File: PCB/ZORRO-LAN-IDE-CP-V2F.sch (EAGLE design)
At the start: 77 parts, among them CN1 ZORROII_EDGE_ROUND_CONTACTS, CN2 A1200-CLOCKPORT, IC1 ENC624J600, IC2 XC95288XL-TQ144, IC3 74HCT245PW, IC4 74HCT245PW, IC5 74HCT245PW, IC7 LD117ADT33TR, IC8 AM29F010S, Q1 25MHz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

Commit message: Update in Firmware (pure Z2-AC but LAN becomes Z3) and new pcb
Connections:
- removed net LAN_CGF2: IC2.P$135-FB6MC02
- net INT6: now also IC2.P$135-FB6MC02
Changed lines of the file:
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@@
 </segment>
 </net>
-<net name="LAN_CGF2" class="0">
+<net name="INT6" class="0">
 <segment>
 <pinref part="IC2" gate="G$1" pin="P$135-FB6MC02"/>

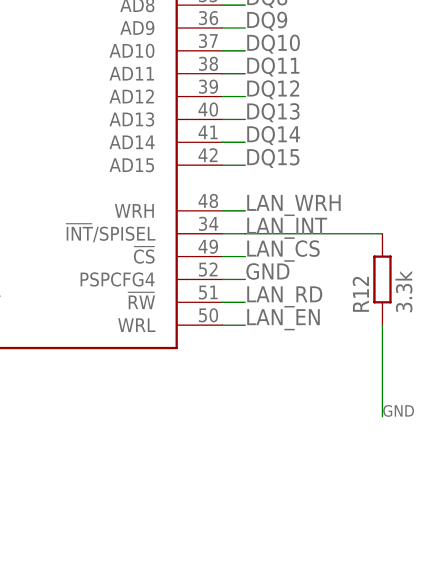
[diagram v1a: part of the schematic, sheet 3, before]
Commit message: Firmware for new version. IDE and CP working
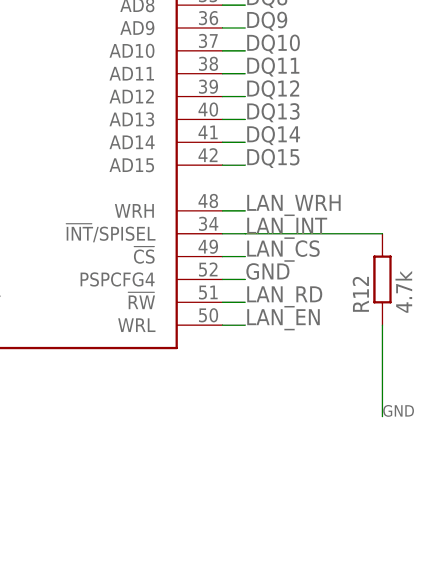
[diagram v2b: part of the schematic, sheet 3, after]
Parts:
- C20, C31: device rcl:C-EUC1210K -> rcl:C-EUC1206K
- R12: value 3.3k -> 4.7k
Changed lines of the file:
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@@
 <?xml version="1.0" encoding="utf-8"?>
 <!DOCTYPE eagle SYSTEM "eagle.dtd">
-<eagle version="6.5.0">
+<eagle version="6.6.0">
 <drawing>
 <settings>
@@
 <grid distance="0.1" unitdist="inch" unit="inch" style="lines" multiple="1" display="no" altdistance="0.01" altunitdist="inch" altunit="inch"/>
 <layers>
-<layer number="1" name="Top" color="4" fill="1" visible="no" active="no"/>
-<layer number="2" name="Route2" color="1" fill="3" visible="no" active="no"/>
-<layer number="3" name="Route3" color="4" fill="3" visible="no" active="no"/>
-<layer number="4" name="Route4" color="1" fill="4" visible="no" active="no"/>
-<layer number="5" name="Route5" color="4" fill="4" visible="no" active="no"/>
-<layer number="6" name="Route6" color="1" fill="8" visible="no" active="no"/>
-<layer number="7" name="Route7" color="4" fill="8" visible="no" active="no"/>
-<layer number="8" name="Route8" color="1" fill="2" visible="no" active="no"/>
-<layer number="9" name="Route9" color="4" fill="2" visible="no" active="no"/>
-<layer number="10" name="Route10" color="1" fill="7" visible="no" active="no"/>
-<layer number="11" name="Route11" color="4" fill="7" visible="no" active="no"/>
-<layer number="12" name="Route12" color="1" fill="5" visible="no" active="no"/>
-<layer number="13" name="Route13" color="4" fill="5" visible="no" active="no"/>
-<layer number="14" name="Route14" color="1" fill="6" visible="no" active="no"/>
-<layer number="15" name="Route15" color="4" fill="6" visible="no" active="no"/>
-<layer number="16" name="Bottom" color="1" fill="1" visible="no" active="no"/>
-<layer number="17" name="Pads" color="2" fill="1" visible="no" active="no"/>
-<layer number="18" name="Vias" color="2" fill="1" visible="no" active="no"/>
-<layer number="19" name="Unrouted" color="6" fill="1" visible="no" active="no"/>
-<layer number="20" name="Dimension" color="15" fill="1" visible="no" active="no"/>
-<layer number="21" name="tPlace" color="7" fill="1" visible="no" active="no"/>
-<layer number="22" name="bPlace" color="7" fill="1" visible="no" active="no"/>
-<layer number="23" name="tOrigins" color="15" fill="1" visible="no" active="no"/>
-<layer number="24" name="bOrigins" color="15" fill="1" visible="no" active="no"/>
-<layer number="25" name="tNames" color="7" fill="1" visible="no" active="no"/>
-<layer number="26" name="bNames" color="7" fill="1" visible="no" active="no"/>
-<layer number="27" name="tValues" color="7" fill="1" visible="no" active="no"/>
-<layer number="28" name="bValues" color="7" fill="1" visible="no" active="no"/>
+<layer number="1" name="Top" color="4" fill="1" visible="yes" active="no"/>
+<layer number="2" name="Route2" color="1" fill="3" visible="yes" active="no"/>
+<layer number="3" name="Route3" color="4" fill="3" visible="yes" active="no"/>
+<layer number="4" name="Route4" color="1" fill="4" visible="yes" active="no"/>
+<layer number="5" name="Route5" color="4" fill="4" visible="yes" active="no"/>
+<layer number="6" name="Route6" color="1" fill="8" visible="yes" active="no"/>
+<layer number="7" name="Route7" color="4" fill="8" visible="yes" active="no"/>
+<layer number="8" name="Route8" color="1" fill="2" visible="yes" active="no"/>
+<layer number="9" name="Route9" color="4" fill="2" visible="yes" active="no"/>
+<layer number="10" name="Route10" color="1" fill="7" visible="yes" active="no"/>
+<layer number="11" name="Route11" color="4" fill="7" visible="yes" active="no"/>
+<layer number="12" name="Route12" color="1" fill="5" visible="yes" active="no"/>
+<layer number="13" name="Route13" color="4" fill="5" visible="yes" active="no"/>
+<layer number="14" name="Route14" color="1" fill="6" visible="yes" active="no"/>
+<layer number="15" name="Route15" color="4" fill="6" visible="yes" active="no"/>
+<layer number="16" name="Bottom" color="1" fill="1" visible="yes" active="no"/>
+<layer number="17" name="Pads" color="2" fill="1" visible="yes" active="no"/>
+<layer number="18" name="Vias" color="2" fill="1" visible="yes" active="no"/>
+<layer number="19" name="Unrouted" color="6" fill="1" visible="yes" active="no"/>
+<layer number="20" name="Dimension" color="15" fill="1" visible="yes" active="no"/>
+<layer number="21" name="tPlace" color="7" fill="1" visible="yes" active="no"/>
+<layer number="22" name="bPlace" color="7" fill="1" visible="yes" active="no"/>
+<layer number="23" name="tOrigins" color="15" fill="1" visible="yes" active="no"/>
+<layer number="24" name="bOrigins" color="15" fill="1" visible="yes" active="no"/>
+<layer number="25" name="tNames" color="7" fill="1" visible="yes" active="no"/>
+<layer number="26" name="bNames" color="7" fill="1" visible="yes" active="no"/>
+<layer number="27" name="tValues" color="7" fill="1" visible="yes" active="no"/>
+<layer number="28" name="bValues" color="7" fill="1" visible="yes" active="no"/>
 <layer number="29" name="tStop" color="7" fill="3" visible="no" active="no"/>
 <layer number="30" name="bStop" color="7" fill="6" visible="no" active="no"/>
@@
 <layer number="35" name="tGlue" color="7" fill="4" visible="no" active="no"/>
 <layer number="36" name="bGlue" color="7" fill="5" visible="no" active="no"/>
-<layer number="37" name="tTest" color="7" fill="1" visible="no" active="no"/>
-<layer number="38" name="bTest" color="7" fill="1" visible="no" active="no"/>
+<layer number="37" name="tTest" color="7" fill="1" visible="yes" active="no"/>
+<layer number="38" name="bTest" color="7" fill="1" visible="yes" active="no"/>
 <layer number="39" name="tKeepout" color="4" fill="11" visible="no" active="no"/>
 <layer number="40" name="bKeepout" color="1" fill="11" visible="no" active="no"/>
@@
 <layer number="44" name="Drills" color="7" fill="1" visible="no" active="no"/>
 <layer number="45" name="Holes" color="7" fill="1" visible="no" active="no"/>
-<layer number="46" name="Milling" color="3" fill="1" visible="no" active="no"/>
-<layer number="47" name="Measures" color="7" fill="1" visible="no" active="no"/>
-<layer number="48" name="Document" color="7" fill="1" visible="no" active="no"/>
-<layer number="49" name="Reference" color="7" fill="1" visible="no" active="no"/>
-<layer number="50" name="dxf" color="7" fill="1" visible="no" active="no"/>
-<layer number="51" name="tDocu" color="7" fill="1" visible="no" active="no"/>
-<layer number="52" name="bDocu" color="7" fill="1" visible="no" active="no"/>
-<layer number="53" name="tGND_GNDA" color="7" fill="1" visible="no" active="no"/>
-<layer number="54" name="bGND_GNDA" color="7" fill="1" visible="no" active="no"/>
-<layer number="56" name="wert" color="7" fill="1" visible="no" active="no"/>
+<layer number="46" name="Milling" color="3" fill="1" visible="yes" active="no"/>
+<layer number="47" name="Measures" color="7" fill="1" visible="yes" active="no"/>
+<layer number="48" name="Document" color="7" fill="1" visible="yes" active="no"/>
+<layer number="49" name="Reference" color="7" fill="1" visible="yes" active="no"/>
+<layer number="50" name="dxf" color="7" fill="1" visible="yes" active="no"/>
+<layer number="51" name="tDocu" color="7" fill="1" visible="yes" active="no"/>
+<layer number="52" name="bDocu" color="7" fill="1" visible="yes" active="no"/>
+<layer number="53" name="tGND_GNDA" color="7" fill="1" visible="yes" active="no"/>
+<layer number="54" name="bGND_GNDA" color="7" fill="1" visible="yes" active="no"/>
+<layer number="56" name="wert" color="7" fill="1" visible="yes" active="no"/>
 <layer number="91" name="Nets" color="2" fill="1" visible="yes" active="yes"/>
 <layer number="92" name="Busses" color="1" fill="1" visible="yes" active="yes"/>
@@
 <part name="GND31" library="supply1" deviceset="GND" device=""/>
 <part name="P+3" library="supply1" deviceset="+5V" device=""/>
-<part name="C20" library="rcl" deviceset="C-EU" device="C1210K" value="10u"/>
+<part name="C20" library="rcl" deviceset="C-EU" device="C1206K" value="10u"/>
 <part name="GND32" library="supply1" deviceset="GND" device=""/>
 <part name="C21" library="rcl" deviceset="C-EU" device="C1210K" value="10u"/>
@@
 <part name="FRAME3" library="frames" deviceset="A4L-LOC" device=""/>
 <part name="R11" library="rcl" deviceset="R-EU_" device="R0805" value="1K"/>
-<part name="R12" library="rcl" deviceset="R-EU_" device="R0603" value="3.3k"/>
+<part name="R12" library="rcl" deviceset="R-EU_" device="R0603" value="4.7k"/>
 <part name="IC1" library="OLIMEX-ENJ" deviceset="ENC624J600" device=""/>
 <part name="C1" library="rcl" deviceset="C-EU" device="C0805K" value="100nF"/>
@@
 <part name="LEDB" library="jumper" deviceset="JP1E" device=""/>
 <part name="LEDA" library="jumper" deviceset="JP1E" device=""/>
-<part name="C31" library="rcl" deviceset="C-EU" device="C1210K" value="47u"/>
+<part name="C31" library="rcl" deviceset="C-EU" device="C1206K" value="47u"/>
 <part name="C32" library="rcl" deviceset="C-EU" device="C0603K" value="100n"/>
 <part name="Q2" library="crystal" deviceset="CRYSTAL" device="HC49UP" value="25MHz"/>

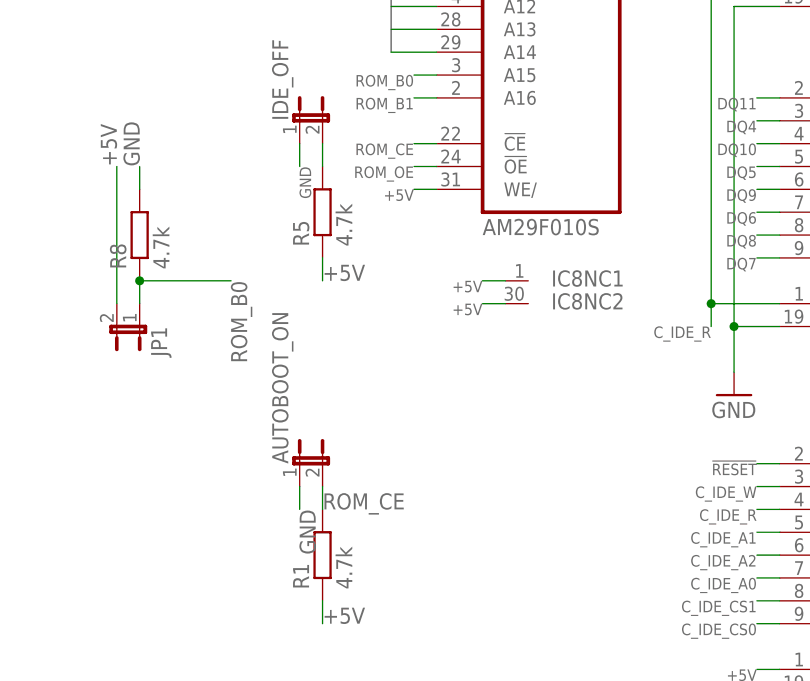
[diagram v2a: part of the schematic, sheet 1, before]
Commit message: Improved clock startup and IDE-ROM-timing
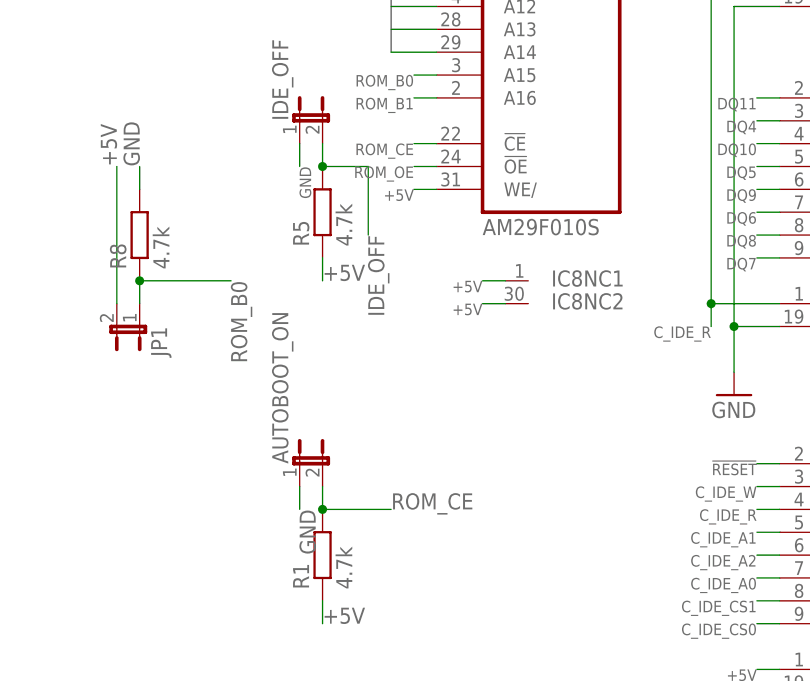
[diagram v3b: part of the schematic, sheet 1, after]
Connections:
- net AUTO_BOOT_OFF renamed IDE_OFF
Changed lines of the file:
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@@
 <grid distance="0.1" unitdist="inch" unit="inch" style="lines" multiple="1" display="no" altdistance="0.01" altunitdist="inch" altunit="inch"/>
 <layers>
-<layer number="1" name="Top" color="4" fill="1" visible="yes" active="no"/>
-<layer number="2" name="Route2" color="1" fill="3" visible="yes" active="no"/>
-<layer number="3" name="Route3" color="4" fill="3" visible="yes" active="no"/>
-<layer number="4" name="Route4" color="1" fill="4" visible="yes" active="no"/>
-<layer number="5" name="Route5" color="4" fill="4" visible="yes" active="no"/>
-<layer number="6" name="Route6" color="1" fill="8" visible="yes" active="no"/>
-<layer number="7" name="Route7" color="4" fill="8" visible="yes" active="no"/>
-<layer number="8" name="Route8" color="1" fill="2" visible="yes" active="no"/>
-<layer number="9" name="Route9" color="4" fill="2" visible="yes" active="no"/>
-<layer number="10" name="Route10" color="1" fill="7" visible="yes" active="no"/>
-<layer number="11" name="Route11" color="4" fill="7" visible="yes" active="no"/>
-<layer number="12" name="Route12" color="1" fill="5" visible="yes" active="no"/>
-<layer number="13" name="Route13" color="4" fill="5" visible="yes" active="no"/>
-<layer number="14" name="Route14" color="1" fill="6" visible="yes" active="no"/>
-<layer number="15" name="Route15" color="4" fill="6" visible="yes" active="no"/>
-<layer number="16" name="Bottom" color="1" fill="1" visible="yes" active="no"/>
-<layer number="17" name="Pads" color="2" fill="1" visible="yes" active="no"/>
-<layer number="18" name="Vias" color="2" fill="1" visible="yes" active="no"/>
-<layer number="19" name="Unrouted" color="6" fill="1" visible="yes" active="no"/>
-<layer number="20" name="Dimension" color="15" fill="1" visible="yes" active="no"/>
-<layer number="21" name="tPlace" color="7" fill="1" visible="yes" active="no"/>
-<layer number="22" name="bPlace" color="7" fill="1" visible="yes" active="no"/>
-<layer number="23" name="tOrigins" color="15" fill="1" visible="yes" active="no"/>
-<layer number="24" name="bOrigins" color="15" fill="1" visible="yes" active="no"/>
-<layer number="25" name="tNames" color="7" fill="1" visible="yes" active="no"/>
-<layer number="26" name="bNames" color="7" fill="1" visible="yes" active="no"/>
-<layer number="27" name="tValues" color="7" fill="1" visible="yes" active="no"/>
-<layer number="28" name="bValues" color="7" fill="1" visible="yes" active="no"/>
+<layer number="1" name="Top" color="4" fill="1" visible="no" active="no"/>
+<layer number="2" name="Route2" color="1" fill="3" visible="no" active="no"/>
+<layer number="3" name="Route3" color="4" fill="3" visible="no" active="no"/>
+<layer number="4" name="Route4" color="1" fill="4" visible="no" active="no"/>
+<layer number="5" name="Route5" color="4" fill="4" visible="no" active="no"/>
+<layer number="6" name="Route6" color="1" fill="8" visible="no" active="no"/>
+<layer number="7" name="Route7" color="4" fill="8" visible="no" active="no"/>
+<layer number="8" name="Route8" color="1" fill="2" visible="no" active="no"/>
+<layer number="9" name="Route9" color="4" fill="2" visible="no" active="no"/>
+<layer number="10" name="Route10" color="1" fill="7" visible="no" active="no"/>
+<layer number="11" name="Route11" color="4" fill="7" visible="no" active="no"/>
+<layer number="12" name="Route12" color="1" fill="5" visible="no" active="no"/>
+<layer number="13" name="Route13" color="4" fill="5" visible="no" active="no"/>
+<layer number="14" name="Route14" color="1" fill="6" visible="no" active="no"/>
+<layer number="15" name="Route15" color="4" fill="6" visible="no" active="no"/>
+<layer number="16" name="Bottom" color="1" fill="1" visible="no" active="no"/>
+<layer number="17" name="Pads" color="2" fill="1" visible="no" active="no"/>
+<layer number="18" name="Vias" color="2" fill="1" visible="no" active="no"/>
+<layer number="19" name="Unrouted" color="6" fill="1" visible="no" active="no"/>
+<layer number="20" name="Dimension" color="15" fill="1" visible="no" active="no"/>
+<layer number="21" name="tPlace" color="7" fill="1" visible="no" active="no"/>
+<layer number="22" name="bPlace" color="7" fill="1" visible="no" active="no"/>
+<layer number="23" name="tOrigins" color="15" fill="1" visible="no" active="no"/>
+<layer number="24" name="bOrigins" color="15" fill="1" visible="no" active="no"/>
+<layer number="25" name="tNames" color="7" fill="1" visible="no" active="no"/>
+<layer number="26" name="bNames" color="7" fill="1" visible="no" active="no"/>
+<layer number="27" name="tValues" color="7" fill="1" visible="no" active="no"/>
+<layer number="28" name="bValues" color="7" fill="1" visible="no" active="no"/>
 <layer number="29" name="tStop" color="7" fill="3" visible="no" active="no"/>
 <layer number="30" name="bStop" color="7" fill="6" visible="no" active="no"/>
@@
 <layer number="35" name="tGlue" color="7" fill="4" visible="no" active="no"/>
 <layer number="36" name="bGlue" color="7" fill="5" visible="no" active="no"/>
-<layer number="37" name="tTest" color="7" fill="1" visible="yes" active="no"/>
-<layer number="38" name="bTest" color="7" fill="1" visible="yes" active="no"/>
+<layer number="37" name="tTest" color="7" fill="1" visible="no" active="no"/>
+<layer number="38" name="bTest" color="7" fill="1" visible="no" active="no"/>
 <layer number="39" name="tKeepout" color="4" fill="11" visible="no" active="no"/>
 <layer number="40" name="bKeepout" color="1" fill="11" visible="no" active="no"/>
@@
 <layer number="44" name="Drills" color="7" fill="1" visible="no" active="no"/>
 <layer number="45" name="Holes" color="7" fill="1" visible="no" active="no"/>
-<layer number="46" name="Milling" color="3" fill="1" visible="yes" active="no"/>
-<layer number="47" name="Measures" color="7" fill="1" visible="yes" active="no"/>
-<layer number="48" name="Document" color="7" fill="1" visible="yes" active="no"/>
-<layer number="49" name="Reference" color="7" fill="1" visible="yes" active="no"/>
-<layer number="50" name="dxf" color="7" fill="1" visible="yes" active="no"/>
-<layer number="51" name="tDocu" color="7" fill="1" visible="yes" active="no"/>
-<layer number="52" name="bDocu" color="7" fill="1" visible="yes" active="no"/>
-<layer number="53" name="tGND_GNDA" color="7" fill="1" visible="yes" active="no"/>
-<layer number="54" name="bGND_GNDA" color="7" fill="1" visible="yes" active="no"/>
-<layer number="56" name="wert" color="7" fill="1" visible="yes" active="no"/>
+<layer number="46" name="Milling" color="3" fill="1" visible="no" active="no"/>
+<layer number="47" name="Measures" color="7" fill="1" visible="no" active="no"/>
+<layer number="48" name="Document" color="7" fill="1" visible="no" active="no"/>
+<layer number="49" name="Reference" color="7" fill="1" visible="no" active="no"/>
+<layer number="50" name="dxf" color="7" fill="1" visible="no" active="no"/>
+<layer number="51" name="tDocu" color="7" fill="1" visible="no" active="no"/>
+<layer number="52" name="bDocu" color="7" fill="1" visible="no" active="no"/>
+<layer number="53" name="tGND_GNDA" color="7" fill="1" visible="no" active="no"/>
+<layer number="54" name="bGND_GNDA" color="7" fill="1" visible="no" active="no"/>
+<layer number="56" name="wert" color="7" fill="1" visible="no" active="no"/>
 <layer number="91" name="Nets" color="2" fill="1" visible="yes" active="yes"/>
 <layer number="92" name="Busses" color="1" fill="1" visible="yes" active="yes"/>
@@
 </segment>
 </net>
-<net name="AUTO_BOOT_OFF" class="0">
+<net name="IDE_OFF" class="0">
 <segment>
 <pinref part="IDE_OFF" gate="A" pin="2"/>
 <pinref part="R5" gate="G$1" pin="2"/>
 <wire x1="119.38" y1="121.92" x2="119.38" y2="119.38" width="0.1524" layer="91"/>
+<label x="124.46" y="111.76" size="1.778" layer="95" rot="R270"/>
+<wire x1="119.38" y1="119.38" x2="124.46" y2="119.38" width="0.1524" layer="91"/>
+<wire x1="124.46" y1="119.38" x2="124.46" y2="111.76" width="0.1524" layer="91"/>
+<junction x="119.38" y="119.38"/>
 </segment>
 </net>
@@
 <pinref part="AUTOBOOT_ON" gate="A" pin="2"/>
 <wire x1="119.38" y1="81.28" x2="119.38" y2="83.82" width="0.1524" layer="91"/>
-<label x="119.38" y="81.28" size="1.778" layer="95"/>
+<label x="127" y="81.28" size="1.778" layer="95"/>
+<wire x1="119.38" y1="81.28" x2="127" y2="81.28" width="0.1524" layer="91"/>
+<junction x="119.38" y="81.28"/>
 </segment>
 </net>
@@
 </segment>
 </net>
-<net name="AUTO_BOOT_OFF" class="0">
+<net name="IDE_OFF" class="0">
 <segment>
 <pinref part="IC2" gate="G$1" pin="P$75-FB13MC11"/>
